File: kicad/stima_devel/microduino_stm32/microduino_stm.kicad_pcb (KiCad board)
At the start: 2 copper layers, 27.9 x 25.4 mm, 19 parts, among them IC1 STM32F103CBT6, J1 Conn_01x01, J2 USB_B_Micro, J3 Conn_01x01, SW1 SW_Push, SW2 SW_Push, Y1 8M, Y2 32.768KHz

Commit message: some modifications and corrections
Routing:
- net GND: track 63.7 -> 39.6 mm, vias 4 -> 2
- net /SDA: track 13.4 -> 12.7 mm, vias 1 -> 2
- net /A7: track 29.6 -> 30.1 mm
- net +3V3: vias 6 -> 8

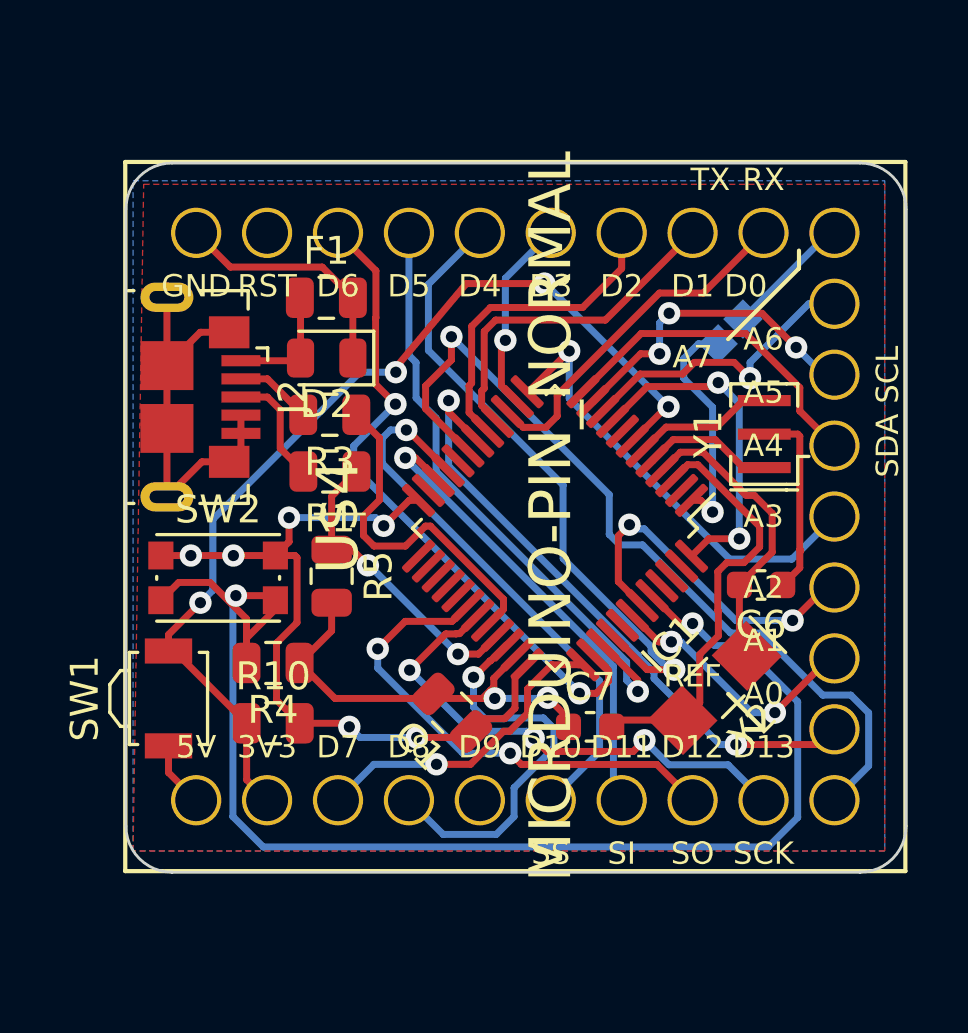
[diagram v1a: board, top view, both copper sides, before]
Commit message: complete redraw pcb after error assignement microduino component
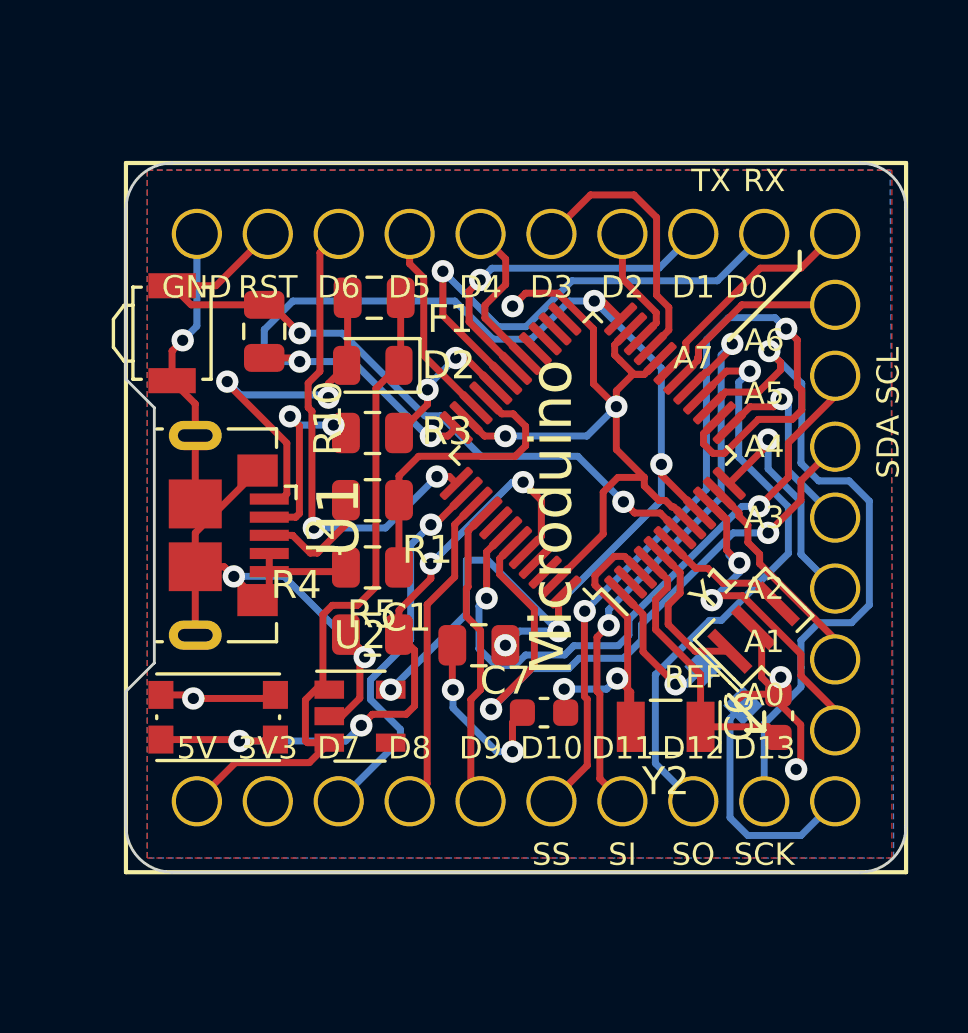
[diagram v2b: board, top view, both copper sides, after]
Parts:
- removed U$4: MICRDUINO-PIN_NORMAL, Microduino:microduino
- added U1: Microduino, Microduino:microduino, F.Cu at (162.2, 167.0)
- added U2: LP2985-3.3, Package_TO_SOT_SMD:SOT-23-5, F.Cu at (155.3, 174.1)
- Y2: footprint Crystal:Crystal_SMD_EuroQuartz_EQ161-2Pin_3.2x1.5mm_HandSoldering -> Crystal:Crystal_SMD_EuroQuartz_EQ161-2Pin_3.2x1.5mm
- moved R10 14.0 mm to (151.9, 160.3), turned to 270 degrees
- moved J1 13.8 mm to (169.0, 173.7)
- moved SW1 13.1 mm to (148.6, 160.4)
- moved J3 11.6 mm to (167.6, 172.3)
- moved Y1 6.94 mm to (169.4, 170.9), turned to 45 degrees
- moved J2 5.06 mm to (150.6, 167.6)
- moved SW2 4.99 mm to (150.2, 174.2)
- moved C6 4.73 mm to (170.3, 174.1), turned to 270 degrees
- moved R4 3.70 mm to (155.8, 171.2), turned to 0 degrees
- moved IC1 2.94 mm to (163.7, 164.8), turned to 135 degrees
- moved C1 2.60 mm to (159.6, 171.6), turned to 180 degrees
- moved Y2 2.24 mm to (166.3, 174.5), turned to 180 degrees
- moved R1 1.84 mm to (155.8, 166.4)
- moved C7 1.73 mm to (161.9, 174.0)
- moved F1 1.71 mm to (155.8, 159.1)
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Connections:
- IC1 pad 29: (no net) -> /D4
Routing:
- net GND: track 39.6 -> 77.9 mm, vias 2 -> 10
- net Net-(IC1-Pad44): track 49.6 -> 24.3 mm, vias 2 -> 4
- net /D10: track 7.01 -> 30.9 mm, vias 1 -> 2
- net /A7: track 30.1 -> 8.12 mm, vias 1 -> 0
- net +3V3: track 40.1 -> 59.8 mm
- net +5V: track 8.74 -> 25.0 mm
- net /A6: track 22.6 -> 6.89 mm, vias 2 -> 0
- net /SCL: track 9.49 -> 23.3 mm
- net /RX3: track 17.0 -> 4.49 mm, vias 1 -> 0
- net /D9: track 22.9 -> 11.1 mm, vias 1 -> 0
- net /SCK: track 12.7 -> 24.5 mm, vias 0 -> 1
- net /SDA: track 12.7 -> 24.4 mm
- net /D8: track 22.0 -> 11.7 mm, vias 1 -> 0
- net /RST: track 36.2 -> 26.1 mm, vias 4 -> 2
- net /D7: track 23.7 -> 13.9 mm, vias 2 -> 1
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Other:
- outline, holes or cut-outs redrawn

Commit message: simplify some tracks
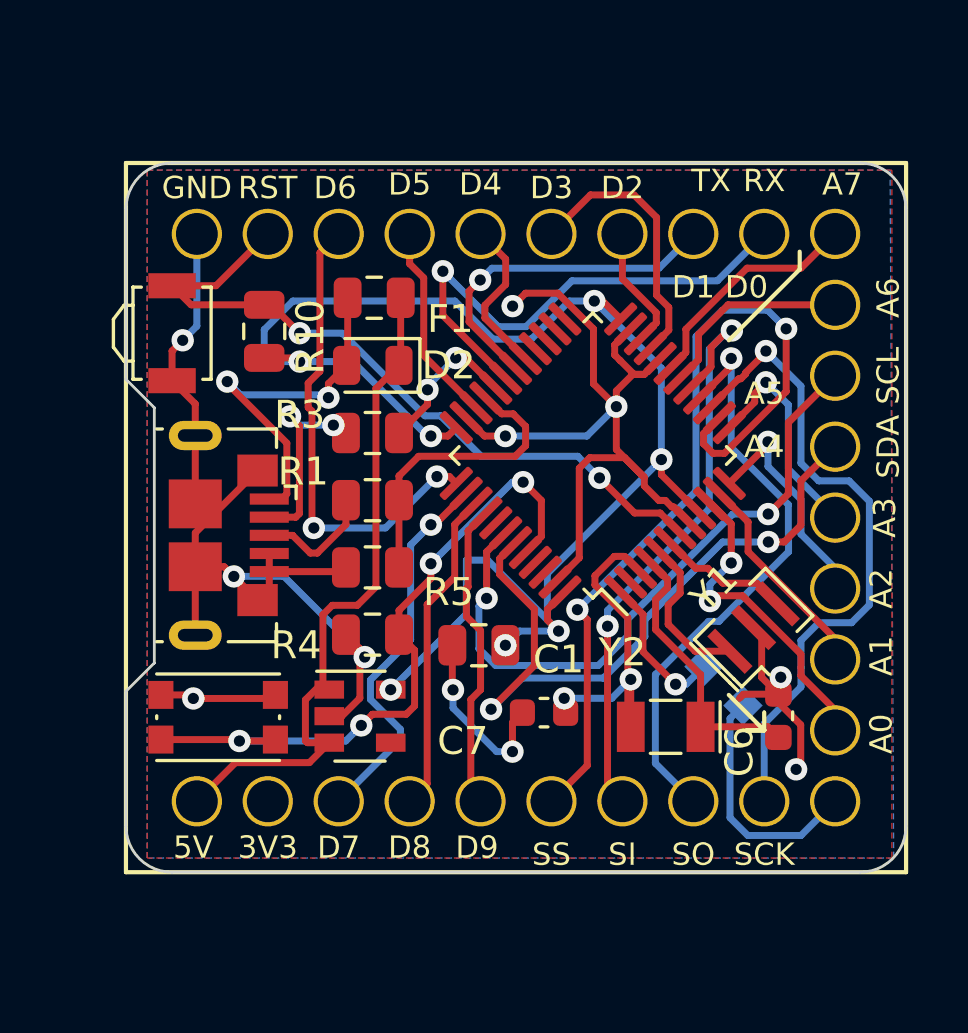
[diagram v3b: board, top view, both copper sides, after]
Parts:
- renumbered J3 to VBAT
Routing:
- net GND: track 77.9 -> 79.4 mm
- net /SCK: track 24.5 -> 23.5 mm
- net +3V3: track 59.8 -> 60.6 mm
- net /MOSI: track 21.0 -> 21.8 mm
- net /A3: track 7.33 -> 8.04 mm
- net /SDA: track 24.4 -> 24.9 mm

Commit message: change solder mask clearance as recommended from oshpark
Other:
- rule pad_to_mask_clearance: 0 -> 0.0508
